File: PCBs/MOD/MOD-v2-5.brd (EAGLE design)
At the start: 100 x 100 mm, 47 parts, among them J1 Teensy-5V, J12 RPi-Shutdown, J17 +5V IN (Main), J3 +5V OUT (to Pi), J4 ACTUATORS, J5 +5V IN (Pi), SW2 500SSP1S2M2QEA, U1 ATTINY85, U2 A2982

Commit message: new boards
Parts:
- renumbered S1A1 to S1-A1, S1A2 to S1-A2, S2A3 to S2-A3, S2A4 to S2-A4, S3A5 to S3-A5, S3A6 to S3-A6, S4A7 to S4-A7, S4A8 to S4-A8, S5A10 to S5-A10, S5A9 to S5-A9, S6A11 to S6-A11, S6A12 to S6-A12
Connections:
- net PWM_1: now also U2.13; no longer U2.20
- net PWM_10: now also U$2.14; no longer U$2.19
- net PWM_11: now also U$2.15; no longer U$2.18
- net PWM_12: now also U$2.16; no longer U$2.17
- net PWM_13: now also U$2.17; no longer U$2.16
- net PWM_14: now also U$2.18; no longer U$2.15
- net PWM_15: now also U$2.19; no longer U$2.14
- net PWM_16: now also U$2.20; no longer U$2.13
- net PWM_2: now also U2.14; no longer U2.19
- net PWM_3: now also U2.15; no longer U2.18
- net PWM_4: now also U2.16; no longer U2.17
- net PWM_5: now also U2.17; no longer U2.16
- net PWM_6: now also U2.18; no longer U2.15
- net PWM_7: now also U2.19; no longer U2.14
- net PWM_8: now also U2.20; no longer U2.13
- net PWM_9: now also U$2.13; no longer U$2.20
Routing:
- net +3V3: track 0.00 -> 479.0 mm, vias 0 -> 10
- net GND: track 0.00 -> 466.7 mm, vias 0 -> 18
- net AGND: track 0.00 -> 407.3 mm, vias 0 -> 13
- net AN10: track 0.00 -> 289.1 mm, vias 0 -> 10
- net AN8: track 0.00 -> 276.2 mm, vias 0 -> 9
- net AN9: track 0.00 -> 269.4 mm, vias 0 -> 12
- net +5V: track 0.00 -> 222.9 mm, vias 0 -> 1
- net AN4: track 0.00 -> 153.7 mm, vias 0 -> 6
- net AN3: track 0.00 -> 145.0 mm, vias 0 -> 4
- net PWM12: track 0.00 -> 137.4 mm, vias 0 -> 8
- net AN5: track 0.00 -> 133.0 mm, vias 0 -> 4
- net AN7: track 0.00 -> 131.6 mm, vias 0 -> 3
- net AN1: track 0.00 -> 130.3 mm, vias 0 -> 5
- net AN2: track 0.00 -> 123.3 mm, vias 0 -> 4
- net AN11: track 0.00 -> 122.2 mm, vias 0 -> 3
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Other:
- board text added: "+5V IN (Main)"
- board text added: "+5V IN (pi)"
- board text added: "+5V OUT (to Pi)"
- board text added: "AN1"
- board text added: "AN10"
- board text added: "AN11"
- board text added: "AN12"
- board text added: "AN2"
- board text added: "AN3"
- board text added: "AN4"
- board text added: "AN5"
- board text added: "AN6"
- board text added: "AN7"
- board text added: "AN8"
- board text added: "AN9"
- board text added: "GND"
- board text added: "VCC"

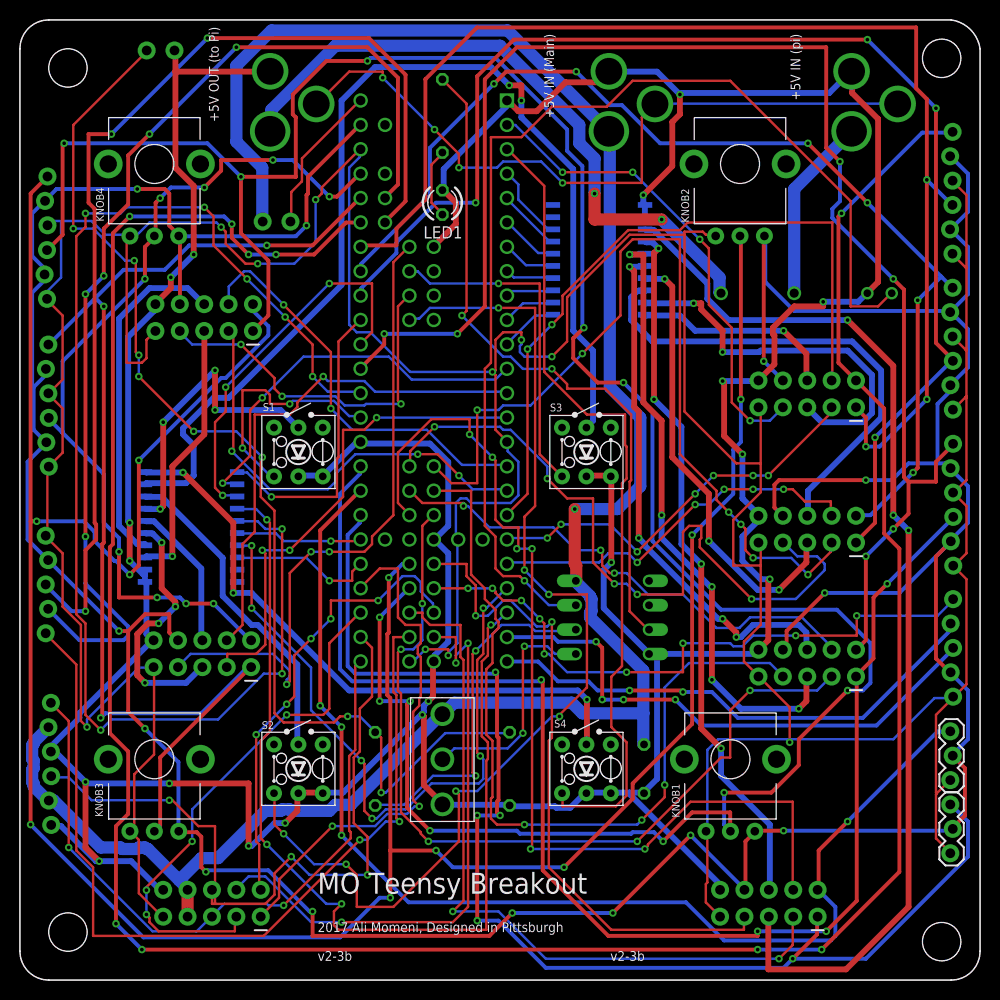
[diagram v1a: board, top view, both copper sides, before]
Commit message: MOD-v2-5 routed
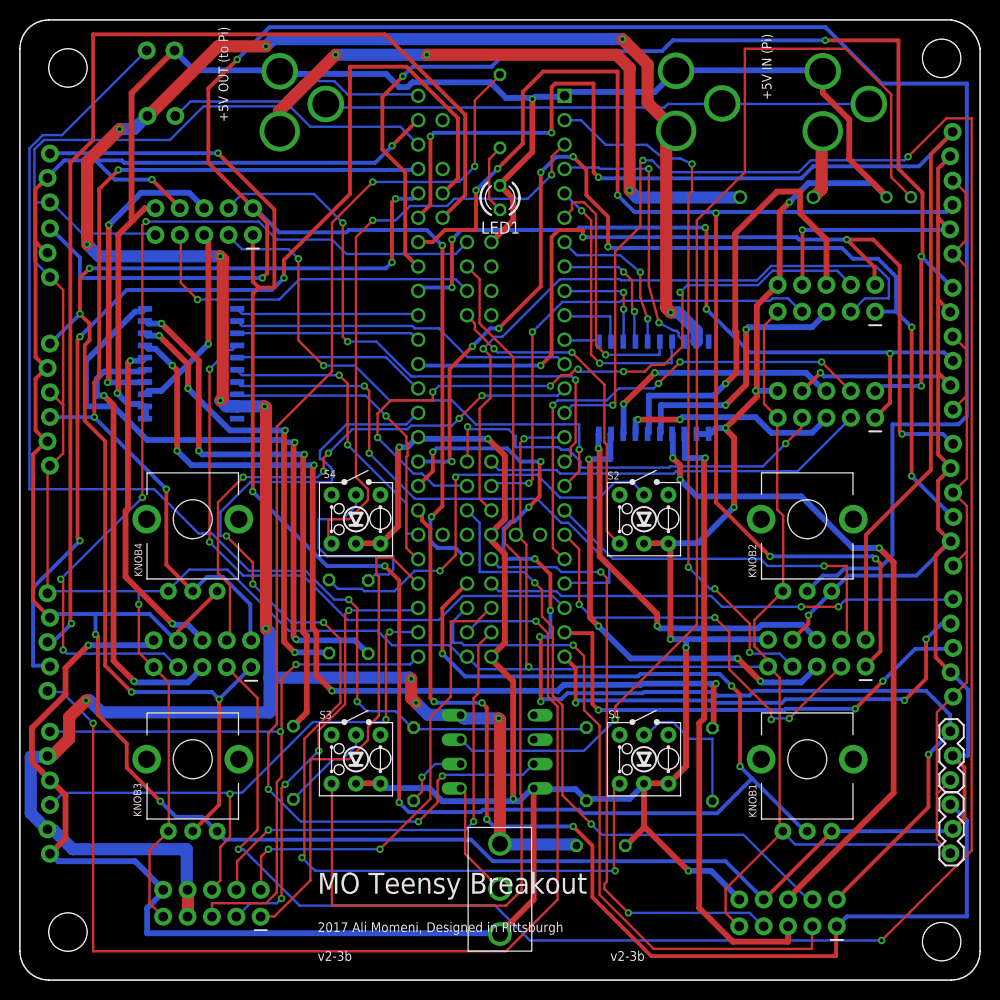
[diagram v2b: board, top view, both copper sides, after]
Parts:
- added R4, R5, R6, R7: 330, rcl:0204/7
- moved S1 48.2 mm to (65.0, 23.0)
- moved S2 44.4 mm to (65.0, 48.0)
- moved S3 40.0 mm to (35.0, 23.0)
- moved STRIP2 38.1 mm to (84.0, 71.0)
- moved KNOB2 37.7 mm to (82.0, 48.0)
- moved KNOB4 37.2 mm to (18.0, 48.0)
- moved S4 35.4 mm to (35.0, 48.0)
- moved STRIP4 27.0 mm to (83.0, 34.1)
- moved U1 18.4 mm to (49.7, 23.8)
- moved U$2 17.0 mm to (17.8, 64.2)
- moved J1 16.3 mm to (16.0, 90.0)
- moved SW2 14.8 mm to (50.0, 9.49)
- moved U2 14.5 mm to (66.0, 61.7), turned to 180 degrees
- moved STRIP3 13.2 mm to (84.0, 60.0)
- moved RELAY1 10.2 mm to (92.8, 81.5)
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- renumbered S1-A1 to S1-AN1, S1-A2 to S1-AN2, S2-A3 to S2-AN3, S2-A4 to S2-AN4, S3-A5 to S3-AN5, S3-A6 to S3-AN6, S4-A7 to S4-AN7, S4-A8 to S4-AN8
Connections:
- new net N$3: R4.2, S1.A
- new net N$4: R5.2, S2.A
- new net N$6: R6.2, S3.A
- new net N$8: R7.2, S4.A
- net PWM_13: now also R4.1; no longer S1.A
- net PWM_14: now also R5.1; no longer S2.A
- net PWM_15: now also R6.1; no longer S3.A
- net PWM_16: now also R7.1; no longer S4.A
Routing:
- net BTN11: track 51.0 -> 250.8 mm, vias 3 -> 5
- net AN8: track 276.2 -> 136.6 mm, vias 9 -> 3
- net PWM12: track 137.4 -> 20.3 mm, vias 8 -> 0
- net BTN13: track 24.9 -> 116.4 mm, vias 2 -> 5
- net BTN14: track 113.1 -> 34.9 mm, vias 7 -> 2
- net AN9: track 269.4 -> 202.6 mm, vias 12 -> 7
- net BTN15: track 35.2 -> 101.2 mm, vias 1 -> 0
- net PWM_13: track 32.0 -> 97.2 mm, vias 4 -> 5
- net AN4: track 153.7 -> 94.5 mm, vias 6 -> 4
- net +5V: track 222.9 -> 280.9 mm, vias 1 -> 13
- net PWM_15: track 112.7 -> 56.9 mm, vias 2 -> 3
- net AN5: track 133.0 -> 79.5 mm, vias 4 -> 5
- net +3V3: track 479.0 -> 426.6 mm, vias 10 -> 3
- net BTN5: track 92.4 -> 40.4 mm, vias 6 -> 0
- net TINY_LED: track 71.4 -> 122.5 mm, vias 2 -> 5
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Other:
- board text added: "+5V IN (Pi)"
- board text removed: "+5V IN (Main)"
- board text removed: "+5V IN (pi)"
- board text removed: "AN10"
- board text removed: "AN11"
- board text removed: "AN12"
- board text removed: "AN9"
